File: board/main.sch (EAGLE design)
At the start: 63 parts, among them J1 HEADER4VALULOK, J2 HEADER6, J3 FUSE, Q1 MOSFET-NCHANNELDFN5X6, Q2 MOSFET-NCHANNELDFN5X6, Q3 MOSFET-NCHANNELDFN5X6, Q4 MOSFET-NCHANNELDFN5X6, Q5 MOSFET-NCHANNELDFN5X6, Q6 MOSFET-NCHANNELDFN5X6, U2 INA181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

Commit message: Pointone update
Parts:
- removed C10: 470uF, SparkFun-Capacitors:1000UF-RADIAL-5MM-25V-20%
- removed C6, C7, C8: 22nF, SparkFun-Capacitors:1.0UF-1206-50V-10%
- added R14, R15, R16, R17, R18, R19: 22, SparkFun-Resistors:RESISTOR1206
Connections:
- new net N$11: Q2.G, R15.2
- new net N$13: Q3.G, R16.2
- new net N$14: Q4.G, R17.2
- new net N$15: Q5.G, R18.2
- new net N$16: Q6.G, R19.2
- new net N$5: Q1.G, R14.2
- net DRV_AH: now also R14.1; no longer Q1.G
- net DRV_AL: now also R15.1; no longer Q2.G
- net DRV_BH: now also R16.1; no longer Q3.G
- net DRV_BL: now also R17.1; no longer Q4.G
- net DRV_CH: now also R18.1; no longer Q5.G
- net DRV_CL: now also R19.1; no longer Q6.G
- net GND: no longer C10.-, C6.2, C7.2, C8.2
- net HALL_A: no longer C6.1
- net HALL_B: no longer C7.1
- net HALL_C: no longer C8.1
- net V_RAW: no longer C10.+
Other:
- note added: "Buck Regulator 60-9v to 5v"
- note removed: "Buck Regulator 60v to 5v"
- moved on the sheet: C1, C15, C16, C18, C19, C2, C20, C3, C4, C5, D1, D2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

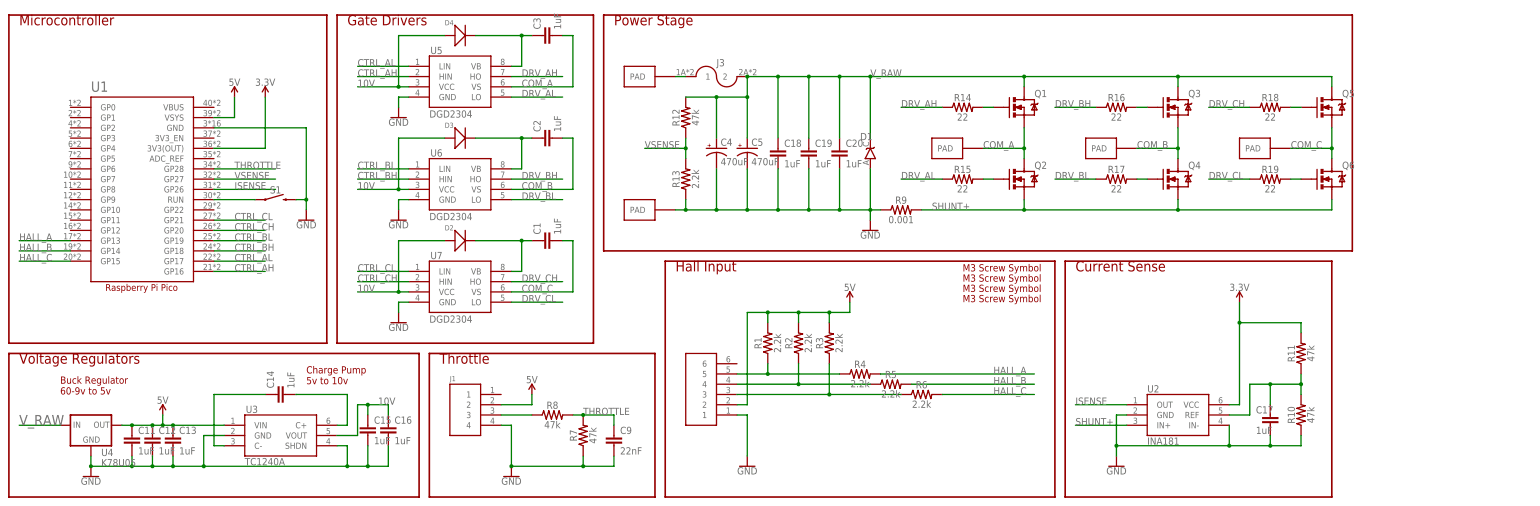
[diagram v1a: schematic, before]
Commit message: 3.2 initial commit, changed FETs to TO-220s
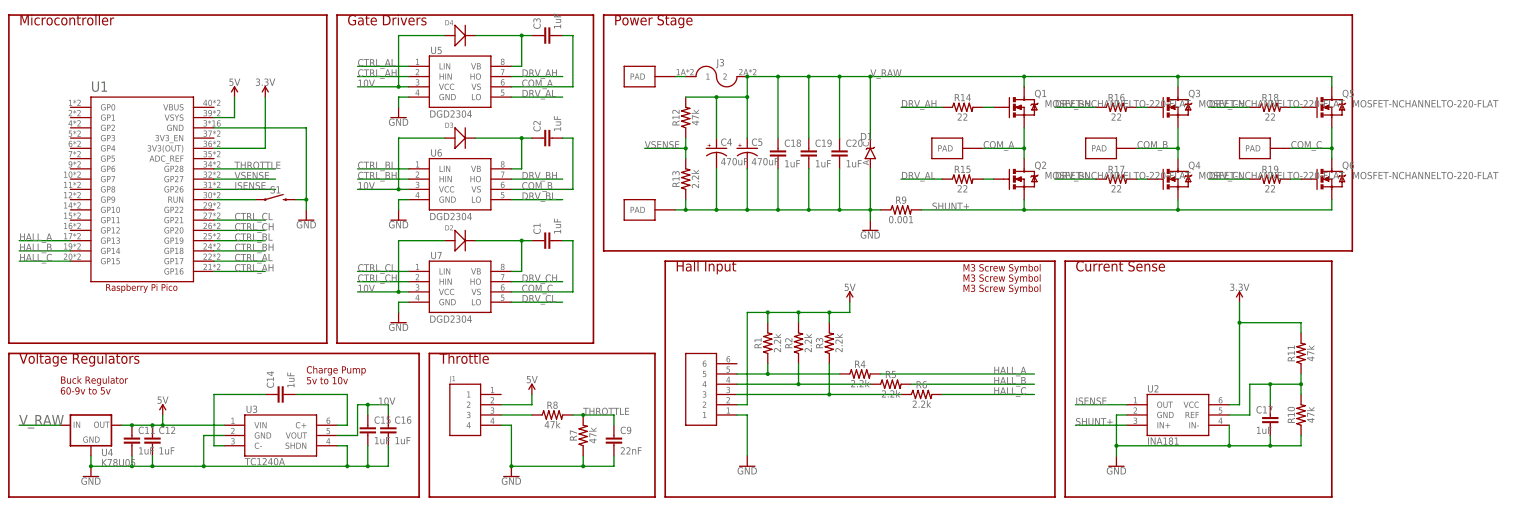
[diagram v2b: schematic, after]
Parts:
- removed C13: 1uF, SparkFun-Capacitors:1.0UF-1206-50V-10%
- removed U$13: SCREW, Custom_old:SCREW
- Q1, Q2, Q3, Q4, Q5, Q6: value MOSFET-NCHANNELDFN5X6 -> MOSFET-NCHANNELTO-220-FLAT; device 2018:MOSFET-NCHANNELDFN5X6 -> Custom_old:MOSFET-NCHANNELTO-220-FLAT
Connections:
- net 5V: no longer C13.1
- net GND: no longer C13.2
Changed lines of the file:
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@@
 <part name="GND1" library="SparkFun-PowerSymbols" deviceset="GND" device=""/>
 <part name="C1" library="SparkFun-Capacitors" deviceset="1.0UF" device="-1206-50V-10%" value="1uF"/>
-<part name="Q1" library="2018" deviceset="MOSFET-NCHANNEL" device="DFN5X6" value=""/>
-<part name="Q2" library="2018" deviceset="MOSFET-NCHANNEL" device="DFN5X6" value=""/>
+<part name="Q1" library="Custom_old" deviceset="MOSFET-NCHANNEL" device="TO-220-FLAT" value="MOSFET-NCHANNELTO-220-FLAT"/>
+<part name="Q2" library="Custom_old" deviceset="MOSFET-NCHANNEL" device="TO-220-FLAT" value="MOSFET-NCHANNELTO-220-FLAT"/>
 <part name="U$4" library="Custom_old" deviceset="PAD" device=""/>
 <part name="U$5" library="Custom_old" deviceset="PAD" device=""/>
 <part name="GND4" library="SparkFun-PowerSymbols" deviceset="GND" device=""/>
-<part name="Q3" library="2018" deviceset="MOSFET-NCHANNEL" device="DFN5X6" value=""/>
-<part name="Q4" library="2018" deviceset="MOSFET-NCHANNEL" device="DFN5X6" value=""/>
-<part name="Q5" library="2018" deviceset="MOSFET-NCHANNEL" device="DFN5X6" value=""/>
-<part name="Q6" library="2018" deviceset="MOSFET-NCHANNEL" device="DFN5X6" value=""/>
+<part name="Q3" library="Custom_old" deviceset="MOSFET-NCHANNEL" device="TO-220-FLAT" value="MOSFET-NCHANNELTO-220-FLAT"/>
+<part name="Q4" library="Custom_old" deviceset="MOSFET-NCHANNEL" device="TO-220-FLAT" value="MOSFET-NCHANNELTO-220-FLAT"/>
+<part name="Q5" library="Custom_old" deviceset="MOSFET-NCHANNEL" device="TO-220-FLAT" value="MOSFET-NCHANNELTO-220-FLAT"/>
+<part name="Q6" library="Custom_old" deviceset="MOSFET-NCHANNEL" device="TO-220-FLAT" value="MOSFET-NCHANNELTO-220-FLAT"/>
 <part name="U$6" library="Custom_old" deviceset="PAD" device="" value="PAD"/>
 <part name="U$7" library="Custom_old" deviceset="PAD" device=""/>
@@
 <part name="U$11" library="Custom_old" deviceset="SCREW" device=""/>
 <part name="U$12" library="Custom_old" deviceset="SCREW" device=""/>
-<part name="U$13" library="Custom_old" deviceset="SCREW" device=""/>
 <part name="C11" library="SparkFun-Capacitors" deviceset="1.0UF" device="-1206-50V-10%" value="1uF"/>
 <part name="C12" library="SparkFun-Capacitors" deviceset="1.0UF" device="-1206-50V-10%" value="1uF"/>
-<part name="C13" library="SparkFun-Capacitors" deviceset="1.0UF" device="-1206-50V-10%" value="1uF"/>
 <part name="R8" library="SparkFun-Resistors" deviceset="RESISTOR" device="1206" value="47k"/>
 <part name="J1" library="Custom_old" deviceset="HEADER4" device="VALULOK"/>
@@
 <instance part="U$11" gate="G$1" x="238.76" y="53.34" smashed="yes"/>
 <instance part="U$12" gate="G$1" x="238.76" y="50.8" smashed="yes"/>
-<instance part="U$13" gate="G$1" x="238.76" y="48.26" smashed="yes"/>
 <instance part="C11" gate="G$1" x="30.48" y="12.7" smashed="yes">
 <attribute name="NAME" x="32.004" y="15.621" size="1.778" layer="95" font="vector"/>
@@
 <attribute name="NAME" x="37.084" y="15.621" size="1.778" layer="95" font="vector"/>
 <attribute name="VALUE" x="37.084" y="10.541" size="1.778" layer="96" font="vector"/>
-</instance>
-<instance part="C13" gate="G$1" x="40.64" y="12.7" smashed="yes">
-<attribute name="NAME" x="42.164" y="15.621" size="1.778" layer="95" font="vector"/>
-<attribute name="VALUE" x="42.164" y="10.541" size="1.778" layer="96" font="vector"/>
 </instance>
 <instance part="R8" gate="G$1" x="134.62" y="20.32" smashed="yes">
@@
 <wire x1="35.56" y1="7.62" x2="35.56" y2="10.16" width="0.1524" layer="91"/>
 <junction x="30.48" y="7.62"/>
-<pinref part="C13" gate="G$1" pin="2"/>
-<wire x1="35.56" y1="7.62" x2="40.64" y2="7.62" width="0.1524" layer="91"/>
-<wire x1="40.64" y1="7.62" x2="40.64" y2="10.16" width="0.1524" layer="91"/>
 <junction x="35.56" y="7.62"/>
-<wire x1="40.64" y1="7.62" x2="48.26" y2="7.62" width="0.1524" layer="91"/>
+<wire x1="35.56" y1="7.62" x2="48.26" y2="7.62" width="0.1524" layer="91"/>
 <wire x1="48.26" y1="7.62" x2="48.26" y2="15.24" width="0.1524" layer="91"/>
-<junction x="40.64" y="7.62"/>
 <pinref part="U3" gate="G$1" pin="GND"/>
 <wire x1="48.26" y1="15.24" x2="53.34" y2="15.24" width="0.1524" layer="91"/>
@@
 <wire x1="30.48" y1="17.78" x2="35.56" y2="17.78" width="0.1524" layer="91"/>
 <junction x="30.48" y="17.78"/>
-<pinref part="C13" gate="G$1" pin="1"/>
 <wire x1="35.56" y1="17.78" x2="38.1" y2="17.78" width="0.1524" layer="91"/>
 <junction x="35.56" y="17.78"/>
 <pinref part="U3" gate="G$1" pin="VIN"/>
-<wire x1="38.1" y1="17.78" x2="40.64" y2="17.78" width="0.1524" layer="91"/>
-<wire x1="40.64" y1="17.78" x2="53.34" y2="17.78" width="0.1524" layer="91"/>
-<junction x="40.64" y="17.78"/>
+<wire x1="38.1" y1="17.78" x2="53.34" y2="17.78" width="0.1524" layer="91"/>
 <pinref part="SUPPLY1" gate="G$1" pin="5V"/>
 <wire x1="38.1" y1="17.78" x2="38.1" y2="20.32" width="0.1524" layer="91"/>

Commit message: Code works
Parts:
- R9: value 0.001 -> 0.0005
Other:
- moved on the sheet: C14, C15, C16, C17, C18, C19, C20, C4, C5, C9, D1, J1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
